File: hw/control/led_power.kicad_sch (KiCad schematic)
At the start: 18 parts, among them U801 LM2678T-ADJ

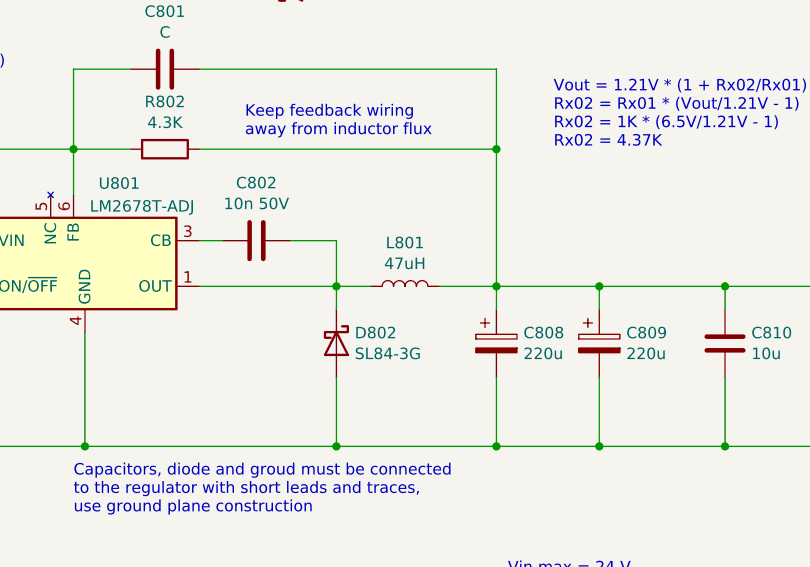
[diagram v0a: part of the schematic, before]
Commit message: [hw] Update to KiCAD 7
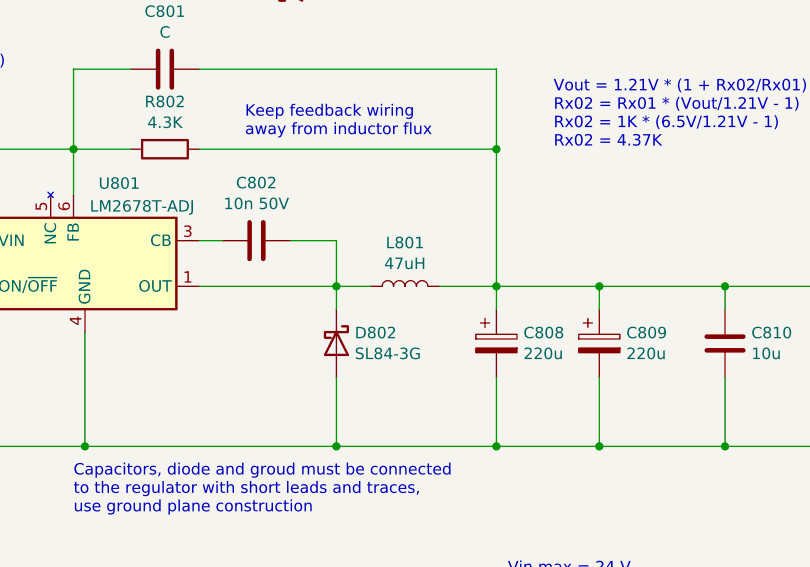
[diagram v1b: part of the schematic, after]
